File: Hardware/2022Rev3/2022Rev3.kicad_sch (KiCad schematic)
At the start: 2 parts

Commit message: circuit addition
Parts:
- added C? (x2): 10uF, symbol Device:C
- added C? (x2): 22uF, symbol Device:C_Polarized_US
- added C? (x2): 1uF, symbol Device:C
- added C?: C, symbol Device:C
- added Conn? (x2): AndersonPP, symbol MRDT_Connectors:AndersonPP
- added D? (x8): D_Schottky, symbol Device:D_Schottky
- added F?: Polyfuse, symbol Device:Polyfuse
- added J? (x2): Conn_01x09, symbol Connector_Generic:Conn_01x09
- added J?: Conn_01x06, symbol Connector_Generic:Conn_01x06
- added J?: RJ45_LED_Shielded, symbol Connector:RJ45_LED_Shielded
- added J?: Conn_01x04, symbol Connector_Generic:Conn_01x04
- added R? (x16): 31.5k, symbol Device:R
- added R? (x16): 40k, symbol Device:R
- added R?: 4k, symbol Device:R
- added R? (x2): 10k, symbol Device:R
- added SW?: SW_SPDT, symbol Switch:SW_SPDT
- added U?: Teensy4.1_DEV-16771, MODULE_DEV-16771, symbol MRDT_Shields:Teensy4.1_DEV-16771
- added U? (x12): Opamp_Dual, symbol Device:Opamp_Dual
- added U? (x2): PESD4USB3U-TBS, symbol BMSRev3:PESD4USB3U-TBS
- added U?: LT1910, symbol MRDT_ICs:LT1910
- added U?: TRS12450, symbol BMSRev3:TRS12433
- added U?: TRS12433, symbol BMSRev3:TRS12433
- added V? (x3): BATT_PWR_VIA, symbol MRDT_Drill_Holes:BATT_PWR_VIA
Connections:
- net +5V: now also C?.1, C?.1, U?.3 (Vout), U?.8 (V+), U?.8 (V+), U?.8 (V+), U?.8 (V+)
- net +BATT: now also U?.4 (IP+), Conn?.2 (V+Log), V?.1; no longer Q?.1 (D)
- net GND: now also C?.2, C?.2, C?.2, C?.2, C?.2, C?.2, C?.2, Conn?.1 (GND), D?.2 (A), J?.1 (Pin_1), J?.1 (Pin_1), J?.4 (Pin_4), R?.1, R?.2, R?.2, R?.2, R?.2, R?.2, R?.2, R?.2, R?.2, R?.2, R?.2, U?.1 (GND), U?.2 (GND), U?.2 (GND), U?.3, U?.3, U?.4 (V-), U?.4 (V-), U?.4 (V-), U?.4 (V-), U?.8, U?.8, U?.GND1 (GND), U?.GND2 (GND), U?.GND3 (GND), U?.GND4 (GND), U?.GND5 (GND), U?.USB_GND1 (USB_GND), U?.USB_GND2 (USB_GND), V?.1
- net PACK_OUT: now reaches Q?.3 (S)
- net PACK_OUT: now also R?.1, V?.1; no longer U?.4 (IP+)
- net at Q?.2 (G): now also U?.5 (GATE)
- net VCC renamed PACK_LOGIC
- net PACK_LOGIC: now also Q?.1 (D), C?.1, F?.1, U?.6 (SENSE), U?.8 (V+)
- new net: U?.3.3V_1 (3.3V), U?.3.3V_2 (3.3V), U?.3.3V_3 (3.3V)
- new net: R?.1, R?.2, U?.6 (-) (x4)
- new net: R?.1, R?.2, U?.2 (-) (x4)
- new net: F?.2, SW?.1 (A)
- new net: C?.1, C?.1, SW?.2 (B), U?.1 (Vin), U?.1 (Vin)
- new net: J?.1, J?.1 (Pin_1)
- new net: R?.1, R?.2, U?.5 (+) (x4)
- new net: R?.1, R?.2, U?.3 (+) (x4)
- new net: U?.10, U?.6, U?.7, U?.9 (x2)
- new net: J?.3 (Pin_3), R?.1, R?.2
- new net: J?.1 (Pin_1), R?.1, U?.4 (IN)
- new net +3V3: C?.1, C?.1, U?.3 (Vout)
- new net GATE: J?.2 (Pin_2)
- new net call6: D?.1 (K), D?.2 (A), J?.4 (Pin_4), J?.4 (Pin_4), R?.1, R?.1, U?.4
- new net cell1: D?.1 (K), D?.2 (A), J?.9 (Pin_9), J?.9 (Pin_9), R?.1, R?.1, U?.5
- new net cell1-sense: R?.2, U?.1, U?.21 (A7)
- new net cell2: D?.1 (K), D?.2 (A), J?.8 (Pin_8), J?.8 (Pin_8), R?.1, R?.1, U?.4
- new net cell2-sense: R?.2, U?.20 (A6), U?.7
- new net cell3: D?.1 (K), D?.2 (A), J?.7 (Pin_7), J?.7 (Pin_7), R?.1, R?.1, U?.2
- new net cell3-sense: R?.2, U?.1, U?.19 (A5)
- new net cell4: D?.1 (K), D?.2 (A), J?.6 (Pin_6), J?.6 (Pin_6), R?.1, R?.1, U?.1
- new net cell4-sense: R?.2, U?.18 (A4), U?.7
- new net cell5: D?.1 (K), D?.2 (A), J?.5 (Pin_5), J?.5 (Pin_5), R?.1, R?.1, U?.5
- new net cell5-sense: R?.2, U?.1, U?.17 (A3)
- new net cell6-sense: R?.2, U?.16 (A2), U?.7
- new net cell7: D?.1 (K), D?.2 (A), J?.3 (Pin_3), J?.3 (Pin_3), R?.1, R?.1, U?.2
- new net cell7-sense: R?.2, U?.1, U?.15 (A1)
- new net cell8: D?.1 (K), J?.2 (Pin_2), J?.2 (Pin_2), R?.1, U?.1
- new net cell8-sense: R?.2, U?.14 (A0), U?.7
- no-connect marks 0 -> 3
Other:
- company: (none) -> Mars Rover Design Team
- title: (none) -> Battery Management System
- moved on the sheet: Q?, U?

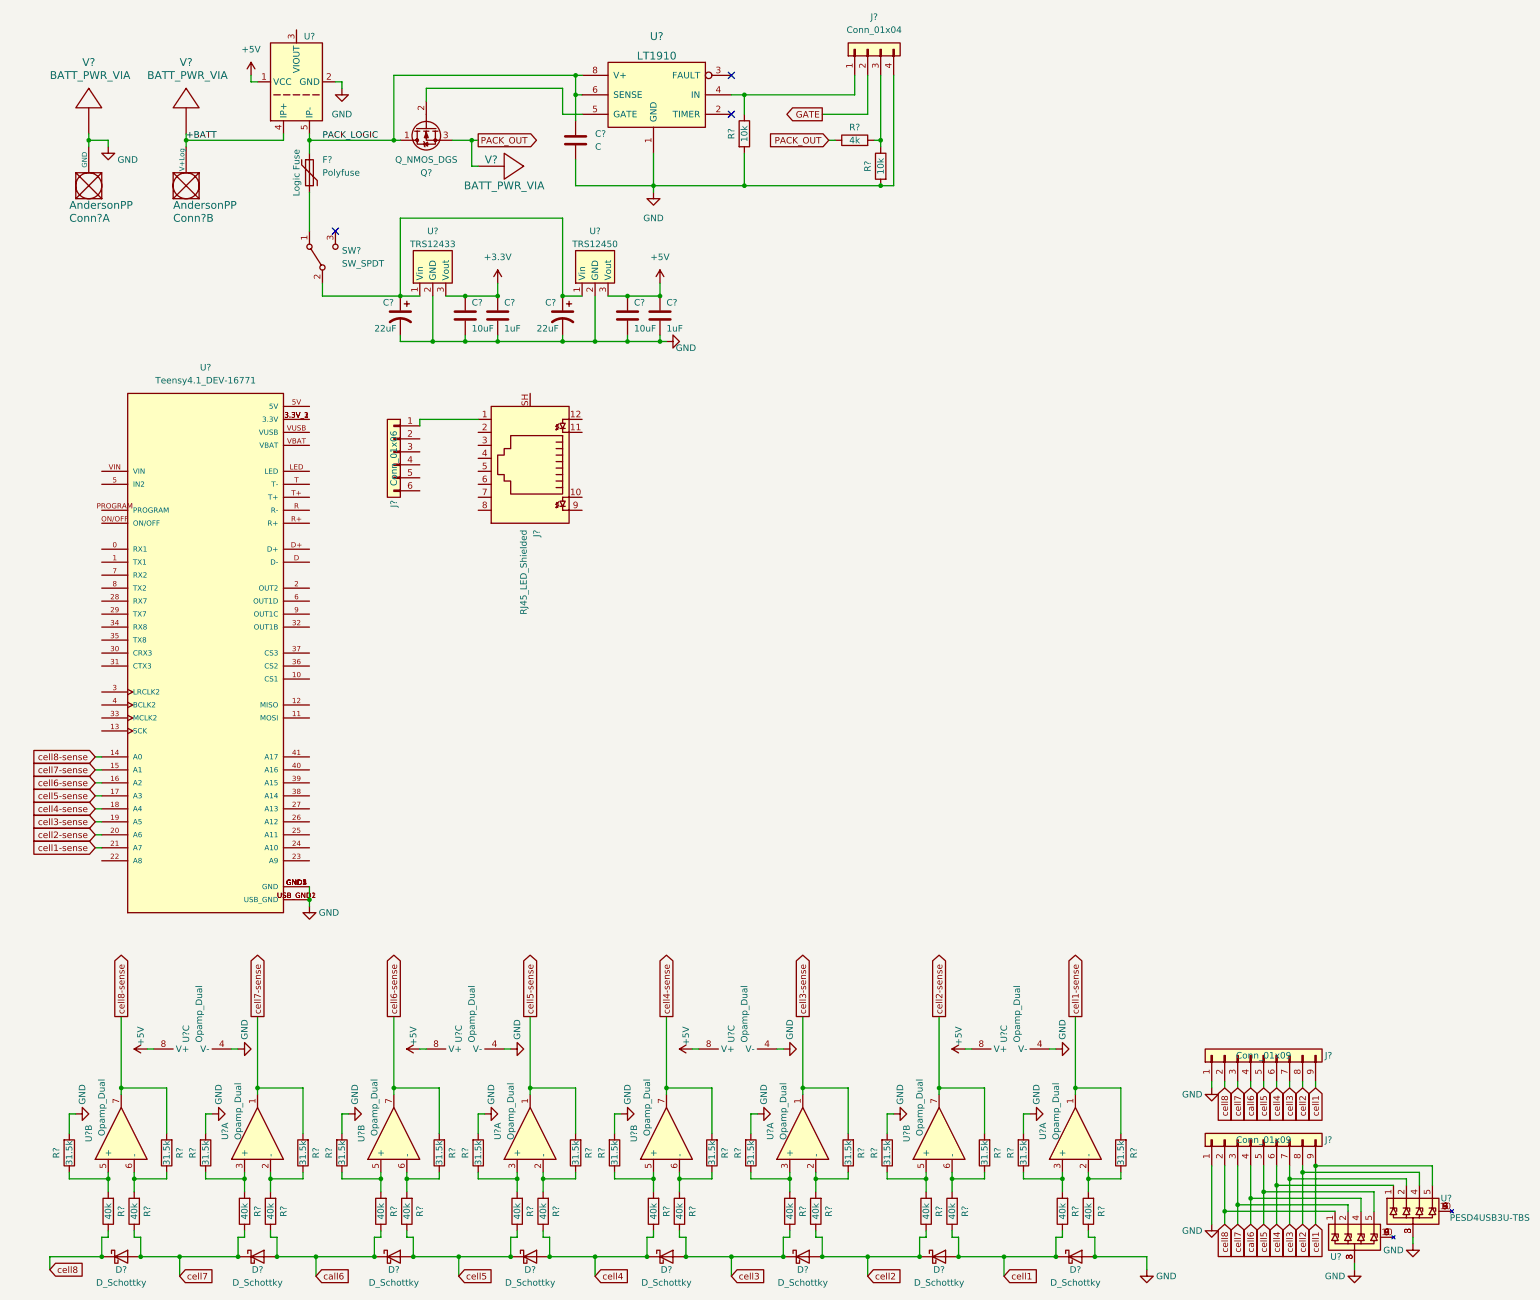
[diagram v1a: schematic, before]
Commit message: LCD, Temp sense, and fan circuits missing. Do layout tomorrow
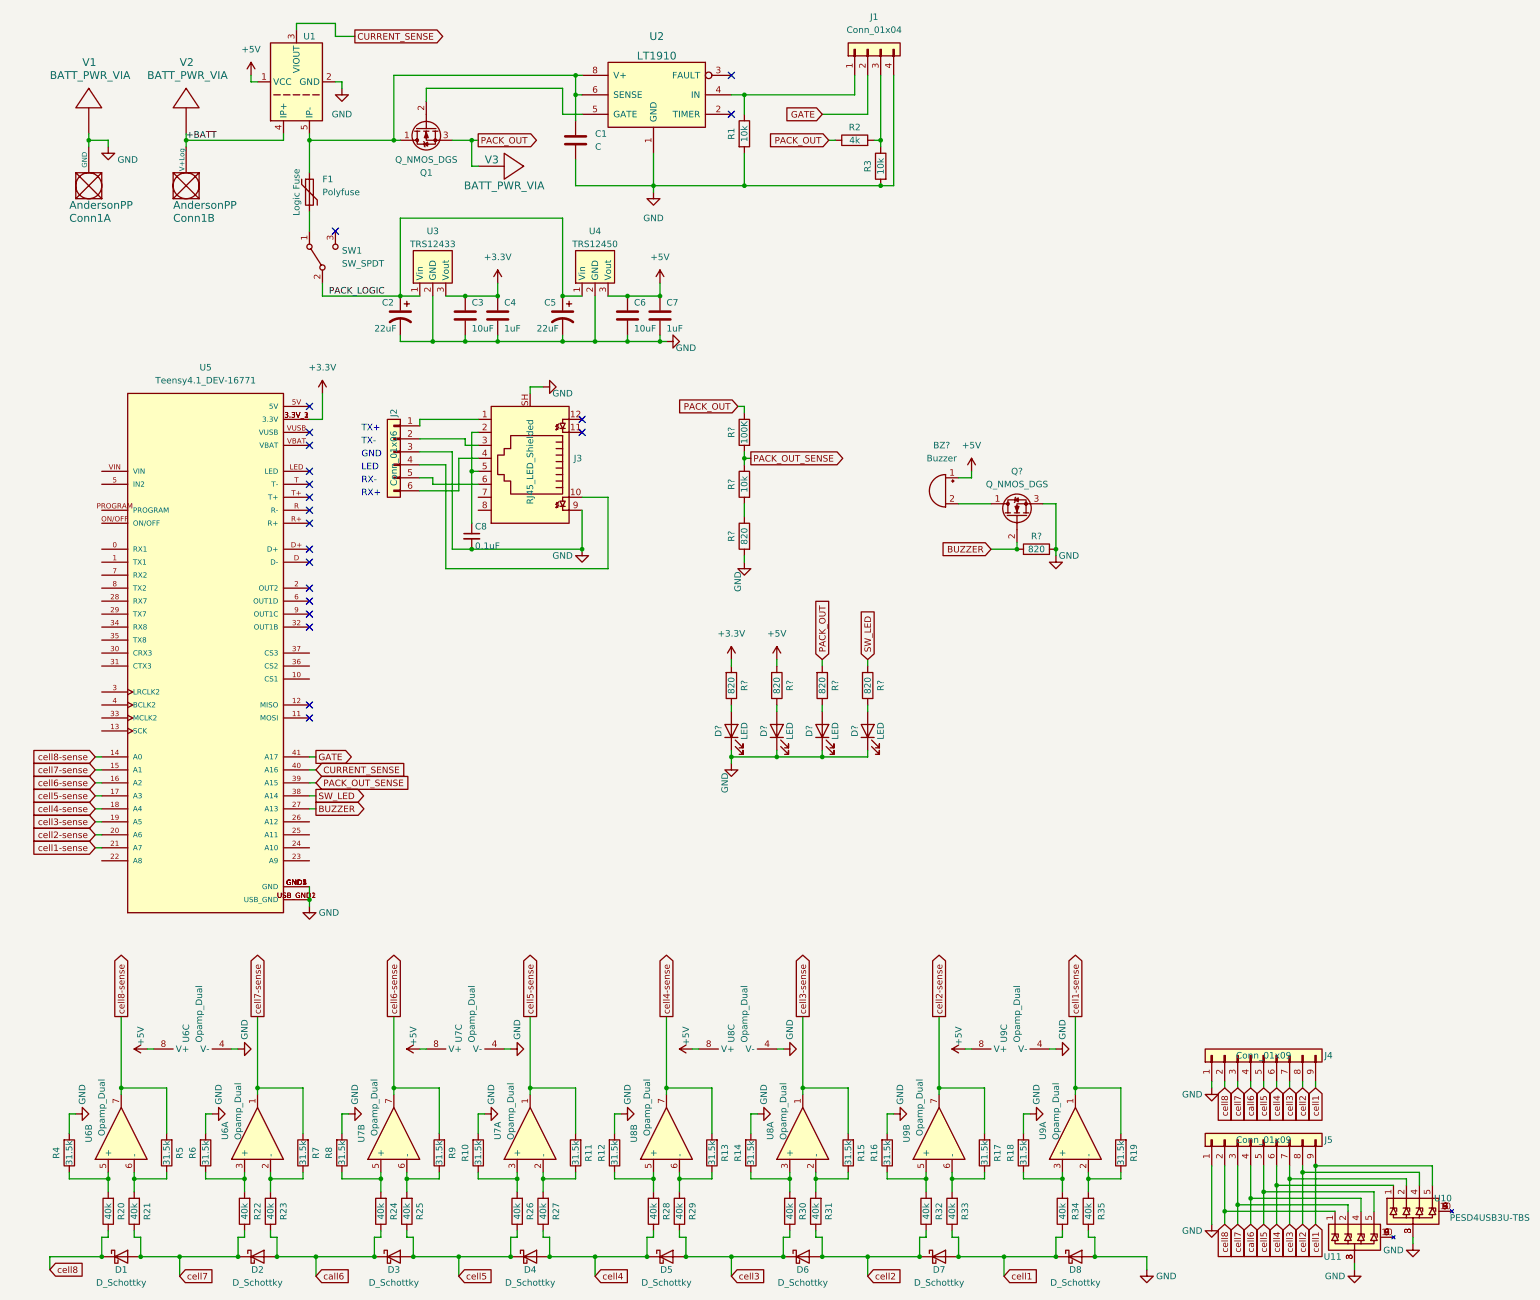
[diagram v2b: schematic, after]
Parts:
- added BZ?: Buzzer, symbol Device:Buzzer
- added C8: 0.1uF, symbol Device:C_Small
- added D? (x4): LED, symbol Device:LED
- added Q?: Q_NMOS_DGS, symbol Device:Q_NMOS_DGS
- added R? (x6): 820, symbol Device:R
- added R?: 100K, symbol Device:R
- added R?: 10k, symbol Device:R
- gave numbers to parts that had none: 73
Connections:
- net +3V3: now also U5.3.3V_1 (3.3V), U5.3.3V_2 (3.3V), U5.3.3V_3 (3.3V), R?.2
- net +5V: now also BZ?.1 (-), R?.2
- net GATE: now also U5.41 (A17)
- net GND: now also J2.3 (Pin_3), J3.9, J3.SH, C8.2, D?.1 (K), D?.1 (K), D?.1 (K), D?.1 (K), Q?.3 (S), R?.1, R?.2
- net PACK_LOGIC: now also C2.1, C5.1, SW1.2 (B), U3.1 (Vin), U4.1 (Vin); no longer C1.1, F1.1, Q1.1 (D), U1.5 (IP-), U2.6 (SENSE), U2.8 (V+)
- net PACK_OUT: now also R?.1, R?.2
- net BUZZER: now reaches U5.27 (A13)
- net BUZZER: now also Q?.2 (G), R?.2
- net SW_LED: now reaches U5.38 (A14)
- net SW_LED: now also R?.2
- net PACK_OUT_SENSE: now reaches U5.39 (A15)
- net PACK_OUT_SENSE: now also R?.1, R?.2
- net CURRENT_SENSE: now reaches U5.40 (A16)
- net CURRENT_SENSE: now also U1.3 (VIOUT)
- net at J2.2 (Pin_2): now also J3.3
- net at J2.4 (Pin_4): now also J3.10
- net at J2.5 (Pin_5): now also J3.6
- net at J2.6 (Pin_6): now also J3.4
- net at J3.2: now also J3.5, C8.1
- new net: D?.2 (A), R?.1 (x4)
- new net: C1.1, F1.1, Q1.1 (D), U1.5 (IP-), U2.6 (SENSE), U2.8 (V+)
- new net: R?.1, R?.2
- new net: BZ?.2 (+), Q?.1 (D)
- no-connect marks 3 -> 21
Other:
- note added: "GND"
- note added: "LED"
- note added: "RX+"
- note added: "RX-"
- note added: "TX+"
- note added: "TX-"
- moved on the sheet: F1
